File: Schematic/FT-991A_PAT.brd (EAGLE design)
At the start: 44.6 x 59.8 mm, 34 parts, among them Q1 PE4259, Q2 MC78L09ABDR2GOSCT, Q3 NLAS4599, Q5 NCP553, Q7 J310, Q8 BFR193F, X1 IF_IN, X2 SCP_OUT, X3 SDR_OUT

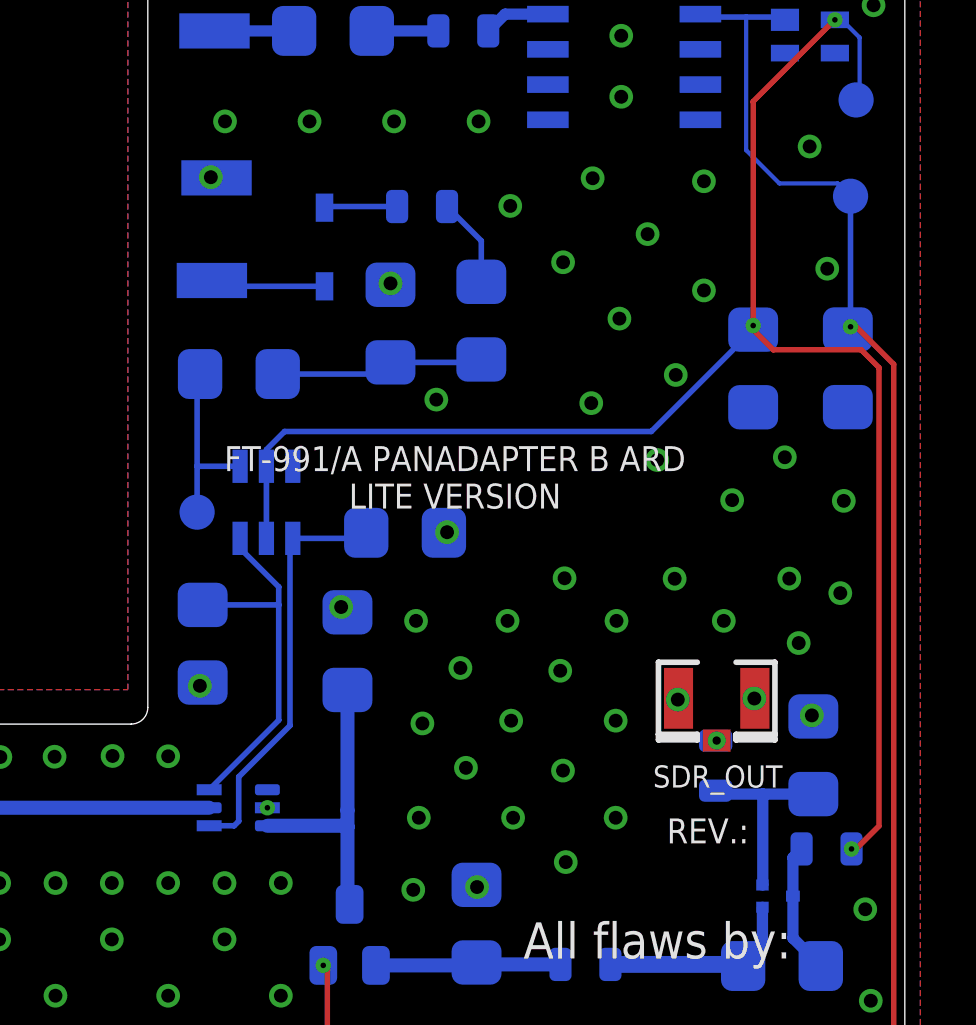
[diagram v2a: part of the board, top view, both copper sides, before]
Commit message: Revision S improvements
- Very minor changes on board design around the power regulator,
  allowing for extra clearance for part description
- Replaced the EOLed OnSemi switch with an active Vishay one
- Updated the overall board block diagram
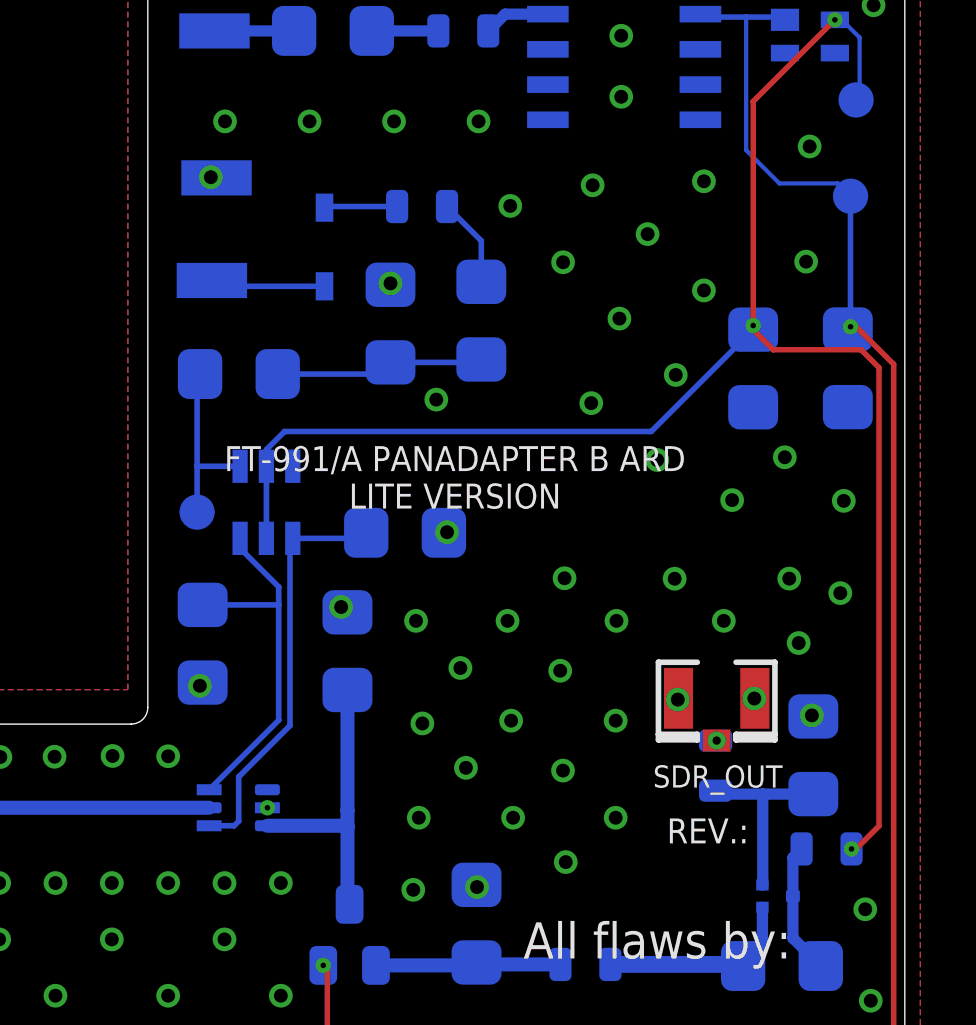
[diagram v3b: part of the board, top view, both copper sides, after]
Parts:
- Q2: value MC78L09ABDR2GOSCT -> MC78L09
- Q3: value NLAS4599 -> DG2001
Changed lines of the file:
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@@
 <drawing>
 <settings>
-<setting alwaysvectorfont="no"/>
+<setting alwaysvectorfont="yes"/>
 <setting keepoldvectorfont="yes"/>
 <setting verticaltext="up"/>
@@
 Laufer, Hugo Marçal (PY2UGO)
 Karl-Arne (SM0AOM)</text>
-<text x="12.016" y="40.65" size="0.9" layer="21" font="vector">&gt;PLOT_DATE_TIME</text>
-<text x="45.3" y="40.9" size="0.9" layer="21" font="vector" rot="R180">REV.:</text>
-<text x="47" y="40.9" size="0.9" layer="29" font="vector" rot="R180">&gt;REVISION_ID</text>
-<text x="34.7" y="53.2" size="0.9" layer="21" font="vector" rot="R180" align="center">FT-991/A PANADAPTER B ARD
+<text x="12.016" y="40.65" size="0.9" layer="21" font="vector" ratio="15">&gt;PLOT_DATE_TIME</text>
+<text x="45.3" y="40.9" size="0.9" layer="21" font="vector" ratio="15" rot="R180">REV.:</text>
+<text x="47" y="40.9" size="1.27" layer="29" font="vector" ratio="15" rot="R180">&gt;REVISION_ID</text>
+<text x="34.7" y="53.2" size="0.9" layer="21" font="vector" ratio="15" rot="R180" align="center">FT-991/A PANADAPTER B ARD
 LITE VERSION</text>
 <text x="42.527" y="51.027" size="1" layer="30" font="vector" ratio="15" rot="MR0" align="center">VAI CORINTHIANS!</text>
@@
 <text x="29.305" y="44.372" size="1.3" layer="29" font="vector" ratio="15" rot="R180" align="center">Light
 Ed</text>
-<text x="47.887" y="66.462" size="0.8" layer="22" font="vector" ratio="15" rot="MR0">3V</text>
+<text x="49.792" y="64.938" size="0.8" layer="22" font="vector" ratio="15" rot="MR0">3V</text>
 <text x="47.684" y="62.773" size="0.8" layer="22" font="vector" ratio="15" rot="MR0">9V</text>
 <text x="25.9" y="50.3" size="0.8" layer="22" font="vector" ratio="15" rot="MR0">sw</text>
-<text x="42" y="34.9" size="1.3" layer="29" font="vector" ratio="15" rot="R180" align="center">PY2RAF</text>
+<text x="42" y="34.392" size="1.3" layer="29" font="vector" ratio="15" rot="R180" align="center">PY2RAF</text>
 <circle x="9.4" y="15.1" radius="1.3038375" width="2.54" layer="29"/>
 <circle x="9.4" y="15.1" radius="1.264909375" width="2.54" layer="30"/>
@@
 </element>
 <element name="Q5" library="aarf" package="SC-82AB" value="NCP553" x="47.5" y="69.1" smashed="yes" rot="MR90">
-<attribute name="VALUE" x="46.84" y="70.76" size="0.8" layer="22" font="vector" ratio="15" rot="MR0" align="center"/>
+<attribute name="VALUE" x="45.318" y="68.684" size="0.8" layer="22" font="vector" ratio="15" rot="MR270" align="center"/>
 </element>
 <element name="F1" library="aarf" package="FUSE-1206" value="50mA" x="30.3" y="69.3" smashed="yes" rot="MR180">
 <attribute name="VALUE" x="30.303" y="67.513" size="0.8" layer="22" font="vector" ratio="15" rot="MR180" align="center"/>
 </element>
-<element name="Q2" library="aarf" package="SOIC8" value="MC78L09ABDR2GOSCT" x="40.8" y="68" smashed="yes" rot="MR270">
+<element name="Q2" library="aarf" package="SOIC8" value="MC78L09" x="40.8" y="68" smashed="yes" rot="MR270">
+<attribute name="VALUE" x="40.927" y="64.952" size="0.8128" layer="22" font="vector" ratio="15" rot="MR0" align="center"/>
 <attribute name="VOLTAGE" value="9V" x="40.8" y="68" size="1.778" layer="28" rot="MR270" display="off"/>
 </element>
@@
 <attribute name="VALUE" x="44.919" y="39.768" size="0.8" layer="22" font="vector" ratio="15" rot="MR0" align="center"/>
 </element>
-<element name="Q3" library="aarf" package="SOT23-6" value="NLAS4599" x="27.9" y="52.3" smashed="yes" rot="MR180">
+<element name="Q3" library="aarf" package="SOT23-6" value="DG2001" x="27.9" y="52.3" smashed="yes" rot="MR180">
 <attribute name="VALUE" x="29.996" y="52.538" size="0.7874" layer="22" font="vector" ratio="15" rot="MR90" align="center"/>
 </element>
@@
 <via x="18.304" y="43.115" extent="1-16" drill="0.5"/>
 <via x="44.395" y="48.025" extent="1-16" drill="0.5"/>
-<via x="39.6648" y="63.9872" extent="1-16" drill="0.5"/>
+<via x="39.6648" y="63.7332" extent="1-16" drill="0.5"/>
 <via x="44.695" y="52.379" extent="1-16" drill="0.5"/>
 <via x="40.695" y="69.125" extent="1-16" drill="0.5"/>
@@
 <via x="27.935" y="41.285" extent="1-16" drill="0.2"/>
 <via x="47.49" y="65.133" extent="1-16" drill="0.5"/>
-<via x="48.125" y="60.725" extent="1-16" drill="0.5"/>
+<via x="47.363" y="60.979" extent="1-16" drill="0.5"/>
 <contactref element="R1" pad="1"/>
 <contactref element="R6" pad="1"/>

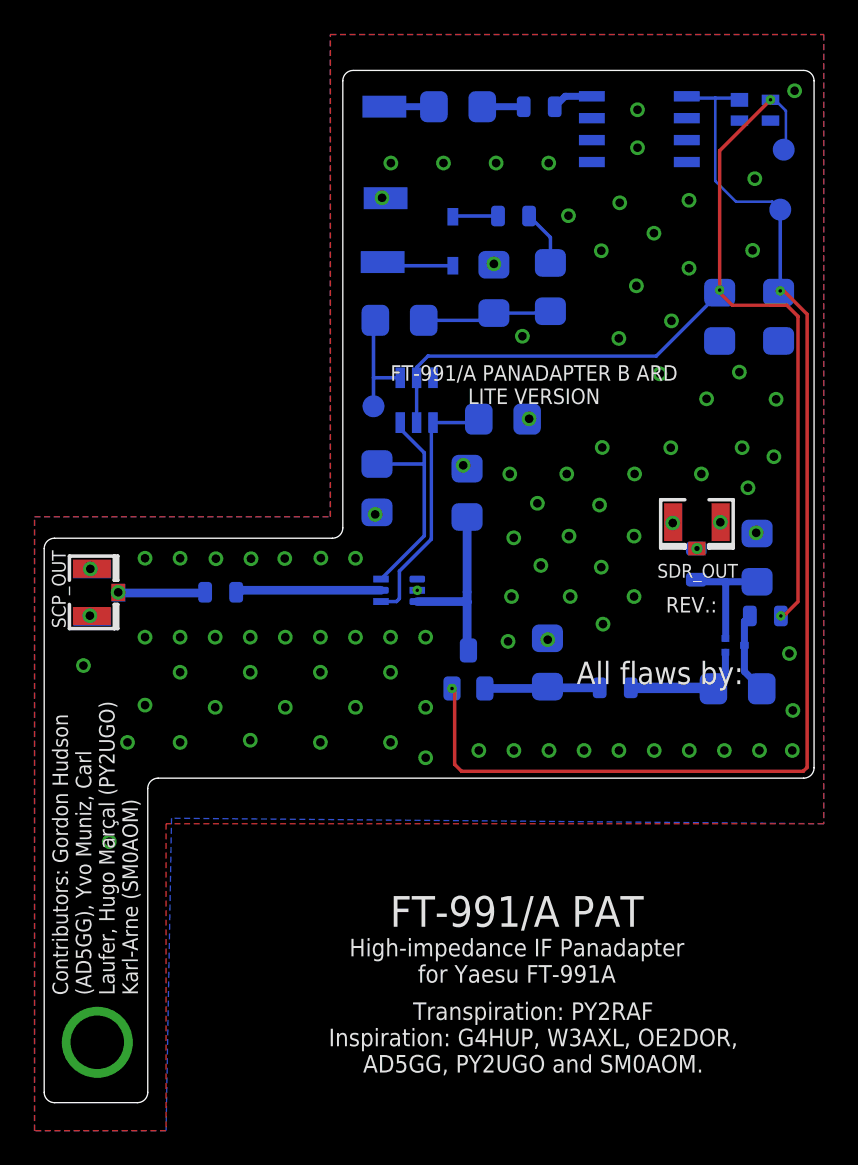
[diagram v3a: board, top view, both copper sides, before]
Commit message: Featuring: Revision T
* Fixed a gross flaw in Revision S: The RF switch was flipped out /o\  Resolves #25
* Updated BOM, renamed some capacitors and the matching network components are labeled as {C,R}1x
* There are more gain to be obtained from BFR193. Added a bias and matching network design from [Infineon's AN-1806](https://www.infineon.com/dgdl/Infineon-Design_Guide_for_low_noise_TR_in_FM_radio_FE-ApplicationNotes-v01_00-EN.pdf?fileId=8ac78c8c7e7124d1017f0227976a6c9d). While the matching network isn't suitable for BFR193, the footprints will be good enough to test other components and values. Capacitors are 0805, Resistors are 1206.
* This revision is planned to be a testbed for a proper bias and match network in order to get better gain figures from BFR193.

Signed-off-by: Rodrigo Freire <py2raf@rf3.org>
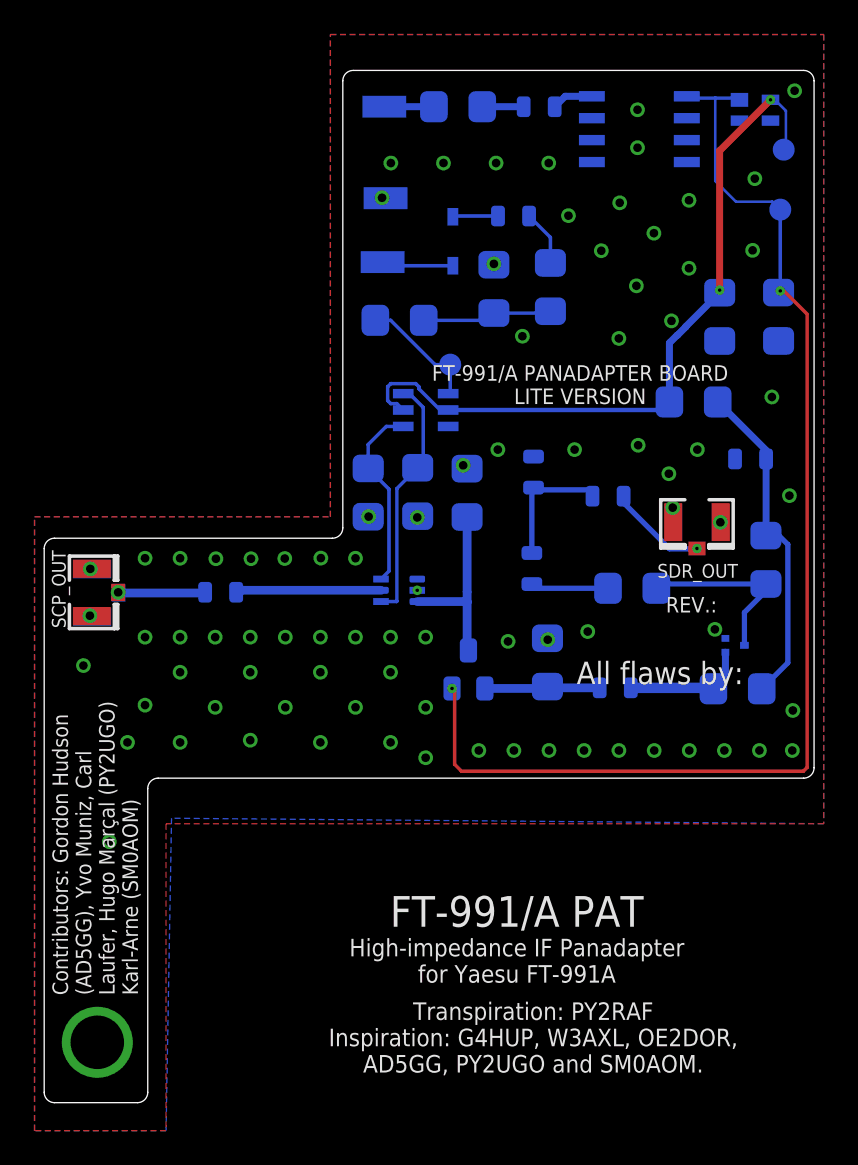
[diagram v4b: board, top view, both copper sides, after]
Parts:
- removed C10: 1000pF, aarf:0805
- removed R10: 220Ω, aarf:1206
- added C12: 330pF, aarf:0805
- added C14: 15pF, aarf:0805
- added C3: 0.1µF, aarf:1206
- added R12: 100Ω, aarf:1206
- added R13, R14: 10Ω, aarf:1206
- C11: value 0.1µF -> 330pF; device aarf:1206 -> aarf:0805
- C13: value 1000pF -> 0.047µF
- L1: value 3.9uH -> 91nH
- R11: value 10kΩ -> 33kΩ
- moved C11 22.3 mm to (39.4, 35.6), turned to 180 degrees
- moved L1 11.5 mm to (39.0, 46.7), turned to 180 degrees
- moved C13 6.86 mm to (47.2, 48.9), turned to 0 degrees
- moved R6 6.50 mm to (28.0, 47.0), turned to 90 degrees
- moved TP3 5.06 mm to (29.8, 54.4)
- moved Q3 0.77 mm to (28.4, 51.7), turned to 270 degrees
- moved R1 0.57 mm to (25.1, 46.9)
- renumbered C7 to C2, R8 to R11
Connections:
- removed net N$2: Q1.4, Q3.4, R6.2
- removed net N$6: Q1.6, Q3.6, R1.2
- new net BIAS: Q8.3, R12.2, R14.1
- new net N$3: C12.P$1, R14.2
- new net NC: Q1.6, Q3.4, R1.2
- new net NO: Q1.4, Q3.6, R6.2
- net 3V: now also C3.1, R13.1; no longer C11.1, L1.P$1
- net FB-3V: now also C13.P$1, R12.1, R13.2; no longer L1.P$2, Q8.3
- net FINAL: now also L1.P$2; no longer C13.P$2
- net GNDA: now also C13.P$2, C14.P$1, C3.2, Q8.2; no longer C11.2, R10.2
- net N$1: now also C12.P$2, C14.P$2, L1.P$1; no longer C13.P$1, Q8.2, R10.1
- net N$4: now also C11.P$2; no longer C10.P$2
- net N$5: now also C11.P$1; no longer C10.P$1
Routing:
- net 3V: track 61.5 -> 42.8 mm, vias 3 -> 2
- net N$2: track 14.9 -> 0.00 mm
- net FB-3V: track 4.77 -> 19.4 mm
- net NO: track 0.00 -> 14.3 mm
- net N$6: track 13.4 -> 0.00 mm
- net NC: track 0.00 -> 11.0 mm
- net BIAS: track 0.00 -> 10.5 mm
- net FINAL: track 0.05 -> 5.74 mm
- net N$3: track 0.00 -> 4.62 mm
- net N$1: track 6.86 -> 7.60 mm
- net N$7: track 6.62 -> 7.14 mm
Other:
- board text added: "FT-991/A PANADAPTER BOARD LITE VERSION"
- board text removed: "FT-991/A PANADAPTER B ARD LITE VERSION"

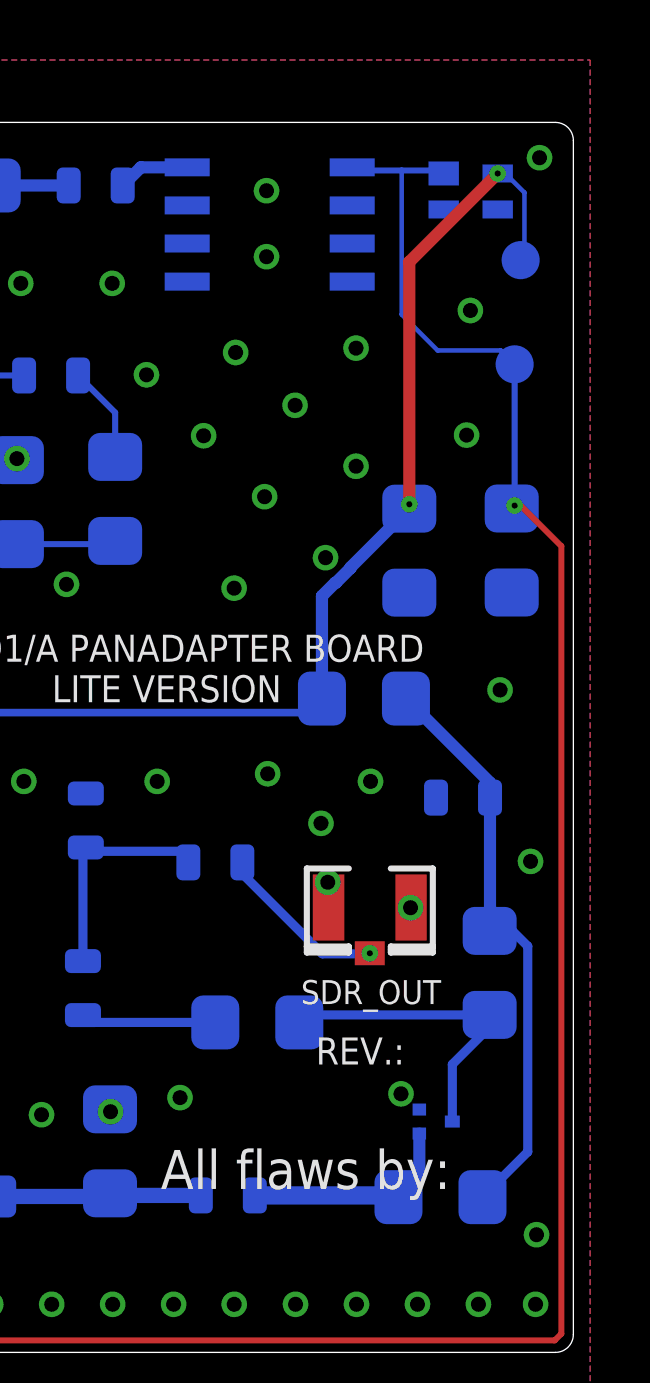
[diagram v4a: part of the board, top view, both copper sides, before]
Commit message: Announcing: Revision U
Featuring:
* A properly matched BFR193F transistor, yielding 7 dB of gain,
  surpassing 2SC5086
* Larger pads for BFR193F
* Few routing improvements, larger wires
* Removed a via near the 3V regulator, didnt help a lot and was
  a short circuit risk.
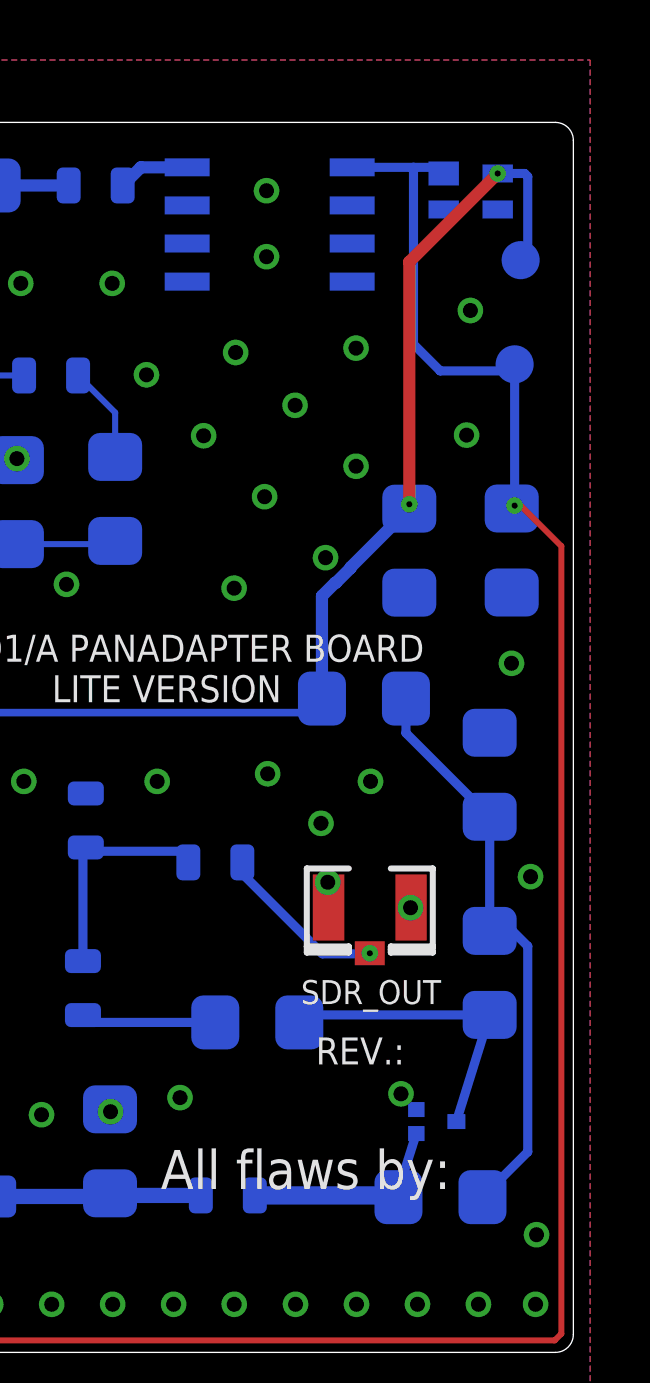
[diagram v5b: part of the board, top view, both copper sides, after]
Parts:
- C11, C12: value 330pF -> 1000pF
- C13: value 0.047µF -> 4.7 nF; device aarf:0805 -> aarf:1206
- C14: value 15pF -> 47pF
- L1: value 91nH -> 82nH
- R11: value 33kΩ -> 39kΩ
- R13: value 10Ω -> 27Ω
- R14: value 10Ω -> 47Ω
- moved C13 1.17 mm to (48.1, 49.7), turned to 90 degrees
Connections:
- net BIAS renamed ST2OUT
- net IFIN renamed ST1IN
- net N$1 renamed ST2M2
- net N$3 renamed ST2M1
- net N$4 renamed ST2IN
- net N$5 renamed ST1M1
- net FB-3V: now also C13.1; no longer C13.P$1
- net GNDA: now also C13.2; no longer C13.P$2
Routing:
- net 9V: track 70.7 -> 71.5 mm
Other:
- board text added: "3x100kΩ"
